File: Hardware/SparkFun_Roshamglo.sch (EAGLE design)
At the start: 38 parts, among them IC1 ATTINY84A, J2 USBPCB, Q1 600mA/40V, U1 IR-Receiver, U3 AP2112K-3.3V

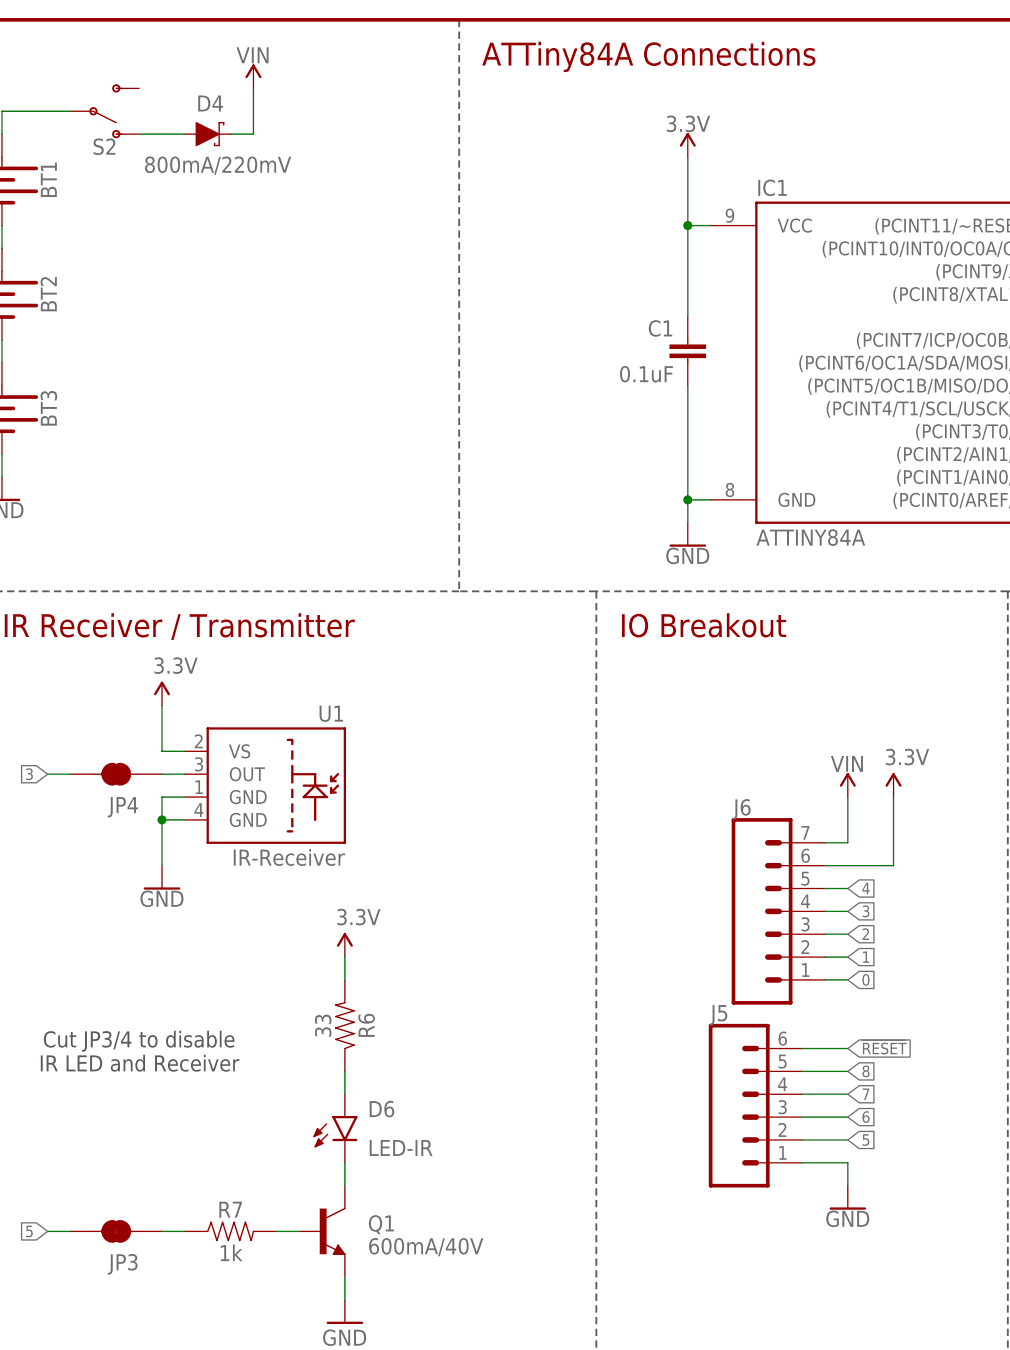
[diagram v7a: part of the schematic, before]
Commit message: v02 changes
Added power LED
Added external parallel resistor
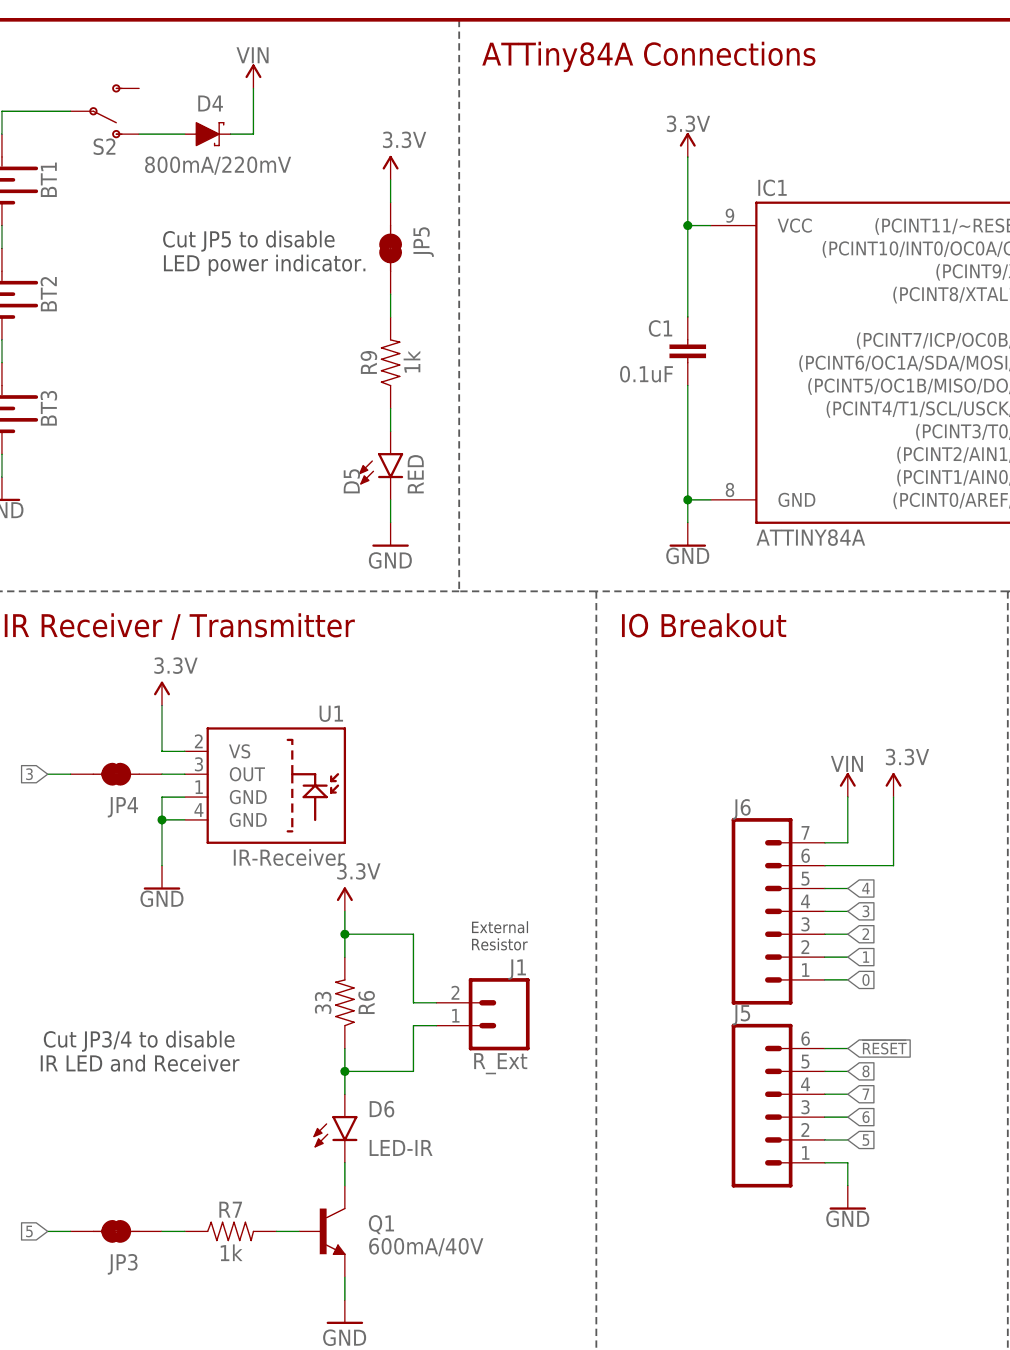
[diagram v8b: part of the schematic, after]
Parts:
- added D5: RED, SparkFun-LED:LED-RED0603
- added J1: R_Ext, SparkFun-Connectors:CONN_021X02_NO_SILK
- added JP5: JUMPER-SMT_2_NC_TRACE_SILK, SparkFun-Jumpers:JUMPER-SMT_2_NC_TRACE_SILK
- added R9: 1k, SparkFun-Resistors:1KOHM-0603-1/10W-1%
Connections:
- new net N$11: JP5.2, R9.2
- new net N$14: D6.A, J1.1, R6.1
- net 3.3V: now also J1.2, JP5.1
- net GND: now also D5.C
- net N$1: now also D5.A, R9.1; no longer D6.A, R6.1
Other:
- note added: "Cut JP5 to disable LED power indicator."
- note added: "External Resistor"
- moved on the sheet: J5, R6
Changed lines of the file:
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@@
 <part name="S3" library="SparkFun-Switches" deviceset="MOMENTARY-SWITCH-SPST" device="-SMD-4.6X2.8MM" value=""/>
 <part name="GND2" library="SparkFun-PowerSymbols" deviceset="GND" device=""/>
+<part name="J1" library="SparkFun-Connectors" deviceset="CONN_02" device="1X02_NO_SILK" value="R_Ext"/>
+<part name="D5" library="SparkFun-LED" deviceset="LED-RED" device="0603" value="RED"/>
+<part name="R9" library="SparkFun-Resistors" deviceset="1KOHM" device="-0603-1/10W-1%" value="1k"/>
+<part name="GND12" library="SparkFun-Aesthetics" deviceset="GND" device=""/>
+<part name="SUPPLY2" library="SparkFun-Aesthetics" deviceset="3.3V" device=""/>
+<part name="JP5" library="SparkFun-Jumpers" deviceset="JUMPER-SMT_2_NC_TRACE" device="_SILK" value=""/>
 </parts>
 <sheets>
@@
 <text x="76.2" y="68.58" size="1.778" layer="97" align="bottom-center">Cut JP3/4 to disable
 IR LED and Receiver</text>
+<text x="113.03" y="82.042" size="1.27" layer="97">External
+Resistor</text>
+<text x="78.74" y="157.48" size="1.778" layer="97">Cut JP5 to disable
+LED power indicator.</text>
 </plain>
 <instances>
@@
 <instance part="SUPPLY9" gate="G$1" x="43.18" y="165.1"/>
 <instance part="SUPPLY13" gate="G$1" x="10.16" y="165.1"/>
-<instance part="R6" gate="G$1" x="99.06" y="73.66" rot="MR90"/>
+<instance part="R6" gate="G$1" x="99.06" y="76.2" rot="MR90"/>
 <instance part="FD1" gate="G$1" x="243.84" y="30.48"/>
 <instance part="FD2" gate="G$1" x="243.84" y="27.94"/>
@@
 <instance part="R7" gate="G$1" x="86.36" y="50.8"/>
 <instance part="GND11" gate="1" x="99.06" y="40.64"/>
-<instance part="SUPPLY7" gate="G$1" x="99.06" y="81.28"/>
-<instance part="J5" gate="G$1" x="144.78" y="63.5"/>
+<instance part="SUPPLY7" gate="G$1" x="99.06" y="86.36"/>
+<instance part="J5" gate="G$1" x="147.32" y="63.5"/>
 <instance part="J6" gate="G$1" x="147.32" y="83.82"/>
 <instance part="GND9" gate="1" x="154.94" y="53.34"/>
@@
 <instance part="S3" gate="G$1" x="205.74" y="162.56"/>
 <instance part="GND2" gate="1" x="213.36" y="157.48"/>
+<instance part="J1" gate="G$1" x="116.84" y="73.66" rot="MR0"/>
+<instance part="D5" gate="G$1" x="104.14" y="137.16"/>
+<instance part="R9" gate="G$1" x="104.14" y="147.32" rot="R90"/>
+<instance part="GND12" gate="1" x="104.14" y="127"/>
+<instance part="SUPPLY2" gate="G$1" x="104.14" y="167.64"/>
+<instance part="JP5" gate="G$1" x="104.14" y="160.02" rot="R270"/>
 </instances>
 <busses>
@@
 <pinref part="R6" gate="G$1" pin="2"/>
 <pinref part="SUPPLY7" gate="G$1" pin="3.3V"/>
-<wire x1="99.06" y1="78.74" x2="99.06" y2="81.28" width="0.1524" layer="91"/>
+<wire x1="99.06" y1="81.28" x2="99.06" y2="83.82" width="0.1524" layer="91"/>
+<wire x1="99.06" y1="83.82" x2="99.06" y2="86.36" width="0.1524" layer="91"/>
+<wire x1="106.68" y1="76.2" x2="106.68" y2="83.82" width="0.1524" layer="91"/>
+<wire x1="106.68" y1="83.82" x2="99.06" y2="83.82" width="0.1524" layer="91"/>
+<junction x="99.06" y="83.82"/>
+<pinref part="J1" gate="G$1" pin="2"/>
+<wire x1="109.22" y1="76.2" x2="106.68" y2="76.2" width="0.1524" layer="91"/>
 </segment>
 <segment>
@@
 <wire x1="193.04" y1="175.26" x2="193.04" y2="177.8" width="0.1524" layer="91"/>
 <pinref part="SUPPLY11" gate="G$1" pin="3.3V"/>
+</segment>
+<segment>
+<pinref part="SUPPLY2" gate="G$1" pin="3.3V"/>
+<pinref part="JP5" gate="G$1" pin="1"/>
+<wire x1="104.14" y1="167.64" x2="104.14" y2="165.1" width="0.1524" layer="91"/>
 </segment>
 </net>
@@
 <segment>
 <pinref part="J5" gate="G$1" pin="1"/>
-<wire x1="149.86" y1="58.42" x2="154.94" y2="58.42" width="0.1524" layer="91"/>
+<wire x1="152.4" y1="58.42" x2="154.94" y2="58.42" width="0.1524" layer="91"/>
 <wire x1="154.94" y1="58.42" x2="154.94" y2="55.88" width="0.1524" layer="91"/>
 <pinref part="GND9" gate="1" pin="GND"/>
@@
 <wire x1="213.36" y1="162.56" x2="213.36" y2="160.02" width="0.1524" layer="91"/>
 <pinref part="GND2" gate="1" pin="GND"/>
+</segment>
+<segment>
+<pinref part="GND12" gate="1" pin="GND"/>
+<pinref part="D5" gate="G$1" pin="C"/>
+<wire x1="104.14" y1="129.54" x2="104.14" y2="132.08" width="0.1524" layer="91"/>
 </segment>
 </net>
@@
 <segment>
 <pinref part="J5" gate="G$1" pin="6"/>
-<wire x1="149.86" y1="71.12" x2="154.94" y2="71.12" width="0.1524" layer="91"/>
+<wire x1="152.4" y1="71.12" x2="154.94" y2="71.12" width="0.1524" layer="91"/>
 <label x="154.94" y="71.12" size="1.27" layer="95" xref="yes"/>
 </segment>
@@
 <segment>
 <pinref part="J5" gate="G$1" pin="5"/>
-<wire x1="149.86" y1="68.58" x2="154.94" y2="68.58" width="0.1524" layer="91"/>
+<wire x1="152.4" y1="68.58" x2="154.94" y2="68.58" width="0.1524" layer="91"/>
 <label x="154.94" y="68.58" size="1.27" layer="95" xref="yes"/>
 </segment>
@@
 <segment>
 <pinref part="J5" gate="G$1" pin="4"/>
-<wire x1="149.86" y1="66.04" x2="154.94" y2="66.04" width="0.1524" layer="91"/>
+<wire x1="152.4" y1="66.04" x2="154.94" y2="66.04" width="0.1524" layer="91"/>
 <label x="154.94" y="66.04" size="1.27" layer="95" xref="yes"/>
 </segment>
@@
 <segment>
 <pinref part="J5" gate="G$1" pin="3"/>
-<wire x1="149.86" y1="63.5" x2="154.94" y2="63.5" width="0.1524" layer="91"/>
+<wire x1="152.4" y1="63.5" x2="154.94" y2="63.5" width="0.1524" layer="91"/>
 <label x="154.94" y="63.5" size="1.27" layer="95" xref="yes"/>
 </segment>
@@
 <segment>
 <pinref part="J5" gate="G$1" pin="2"/>
-<wire x1="149.86" y1="60.96" x2="154.94" y2="60.96" width="0.1524" layer="91"/>
+<wire x1="152.4" y1="60.96" x2="154.94" y2="60.96" width="0.1524" layer="91"/>
 <label x="154.94" y="60.96" size="1.27" layer="95" xref="yes"/>
 </segment>
@@
 </segment>
 </net>
-<net name="N$1" class="0">
-<segment>
-<pinref part="R6" gate="G$1" pin="1"/>
-<pinref part="D6" gate="G$1" pin="A"/>
-<wire x1="99.06" y1="68.58" x2="99.06" y2="66.04" width="0.1524" layer="91"/>
-</segment>
-</net>
 <net name="N$3" class="0">
 <segment>
@@
 </segment>
 </net>
+<net name="N$14" class="0">
+<segment>
+<wire x1="106.68" y1="73.66" x2="106.68" y2="68.58" width="0.1524" layer="91"/>
+<pinref part="R6" gate="G$1" pin="1"/>
+<pinref part="D6" gate="G$1" pin="A"/>
+<wire x1="99.06" y1="71.12" x2="99.06" y2="68.58" width="0.1524" layer="91"/>
+<wire x1="99.06" y1="68.58" x2="99.06" y2="66.04" width="0.1524" layer="91"/>
+<wire x1="106.68" y1="68.58" x2="99.06" y2="68.58" width="0.1524" layer="91"/>
+<junction x="99.06" y="68.58"/>
+<pinref part="J1" gate="G$1" pin="1"/>
+<wire x1="106.68" y1="73.66" x2="109.22" y2="73.66" width="0.1524" layer="91"/>
+</segment>
+</net>
+<net name="N$1" class="0">
+<segment>
+<pinref part="D5" gate="G$1" pin="A"/>
+<pinref part="R9" gate="G$1" pin="1"/>
+<wire x1="104.14" y1="139.7" x2="104.14" y2="142.24" width="0.1524" layer="91"/>
+</segment>
+</net>
+<net name="N$11" class="0">
+<segment>
+<pinref part="JP5" gate="G$1" pin="2"/>
+<pinref part="R9" gate="G$1" pin="2"/>
+<wire x1="104.14" y1="154.94" x2="104.14" y2="152.4" width="0.1524" layer="91"/>
+</segment>
+</net>
